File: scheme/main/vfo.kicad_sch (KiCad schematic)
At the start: 20 parts, among them Q1 BC847, U10 HCPL-817-50CE, U11 RS8551, U8 AMC1311, U9 RS8551

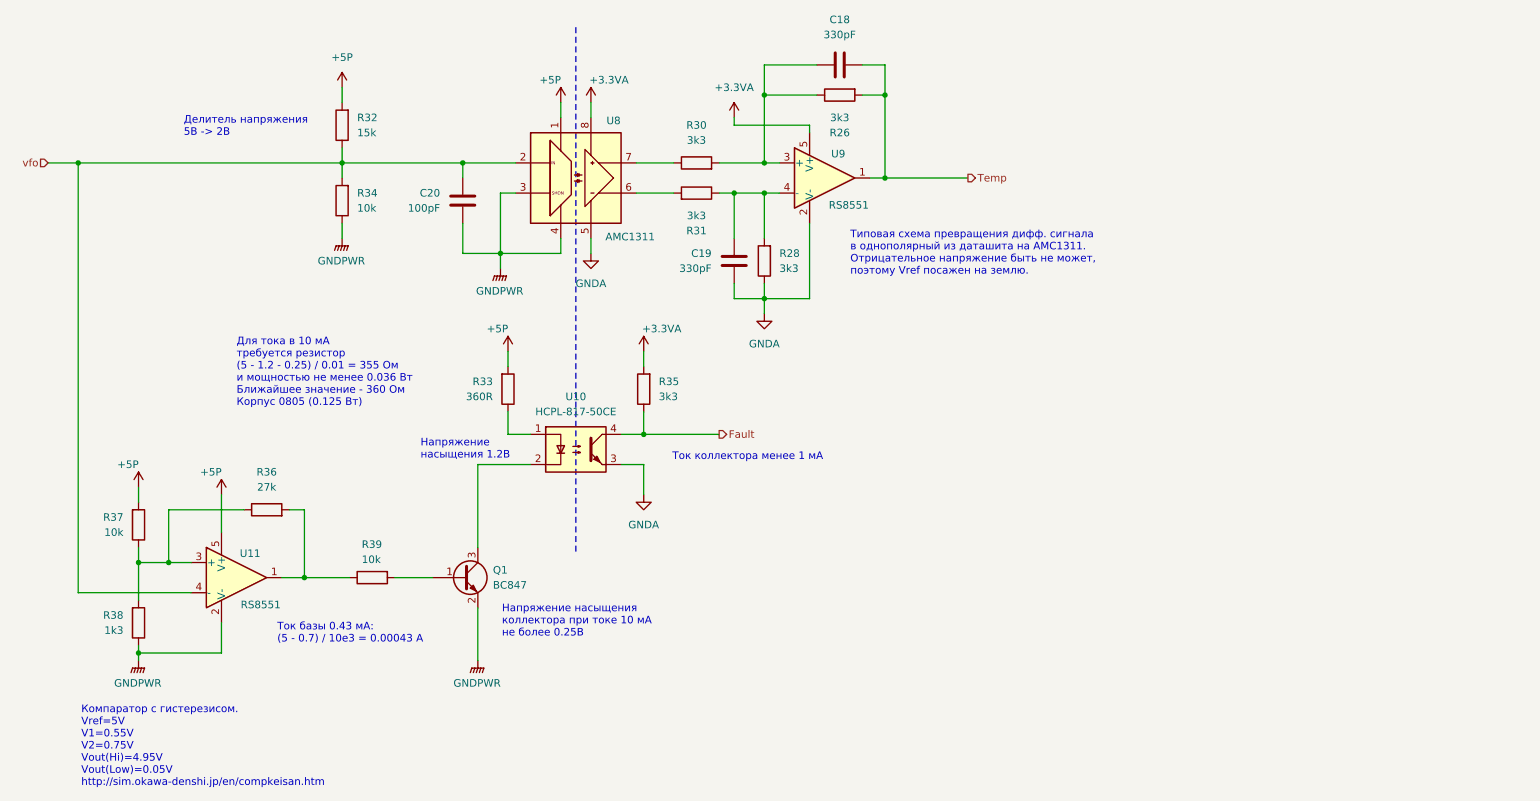
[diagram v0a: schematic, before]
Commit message: vdc meas scheme
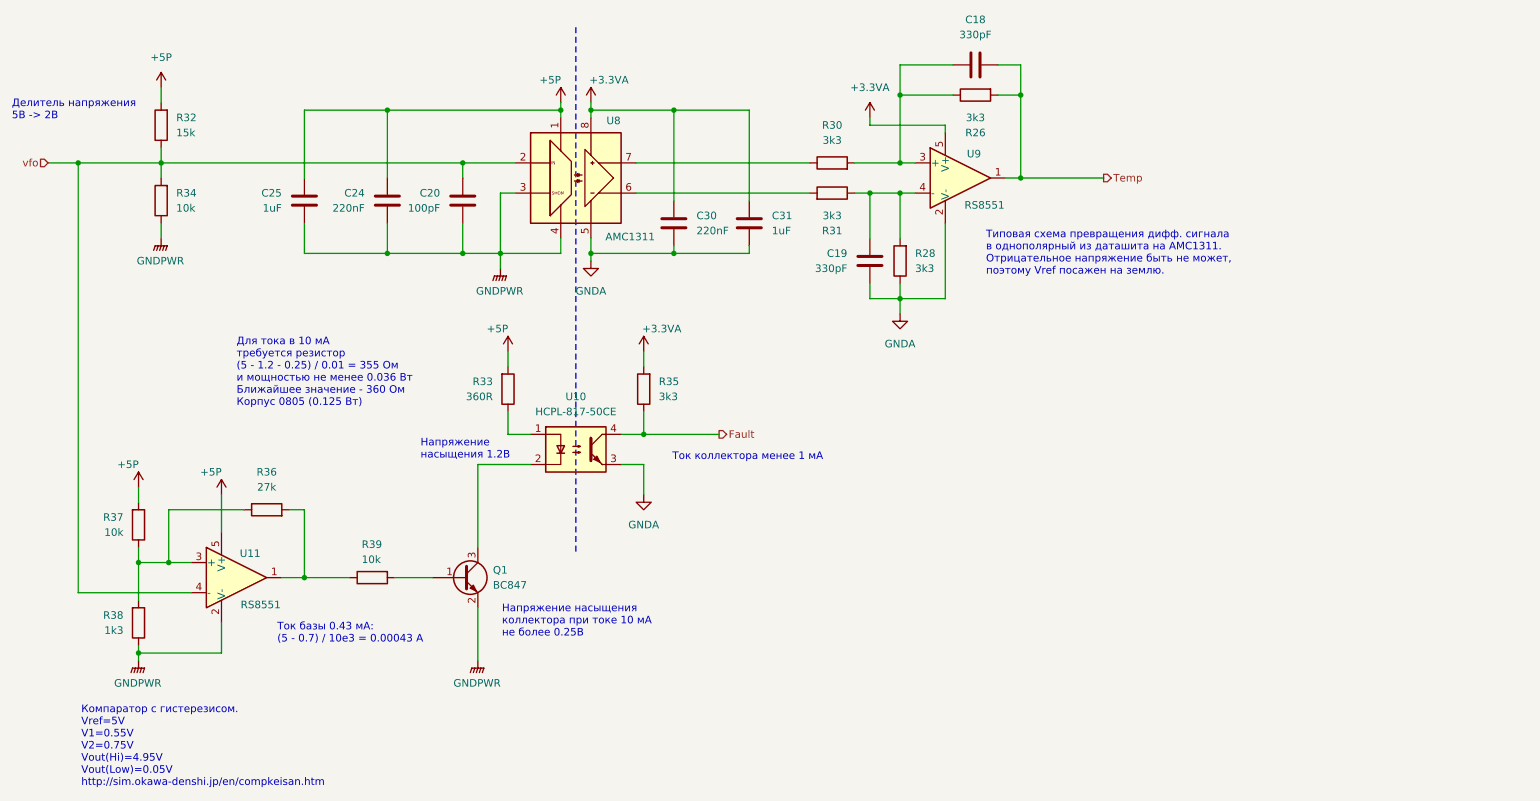
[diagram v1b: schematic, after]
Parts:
- added C24, C30: 220nF, Capacitor_SMD:C_0805_2012Metric, symbol Device:C
- added C25, C31: 1uF, Capacitor_SMD:C_0805_2012Metric, symbol Device:C
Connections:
- net +3.3VA: now also C30.1, C31.1
- net +5P: now also C24.1, C25.1
- net GNDA: now also C30.2, C31.2
- net GNDPWR: now also C24.2, C25.2
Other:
- moved on the sheet: C18, C19, R26, R28, R30, R31, R32, R34, U9

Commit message: added decoupling capacitors
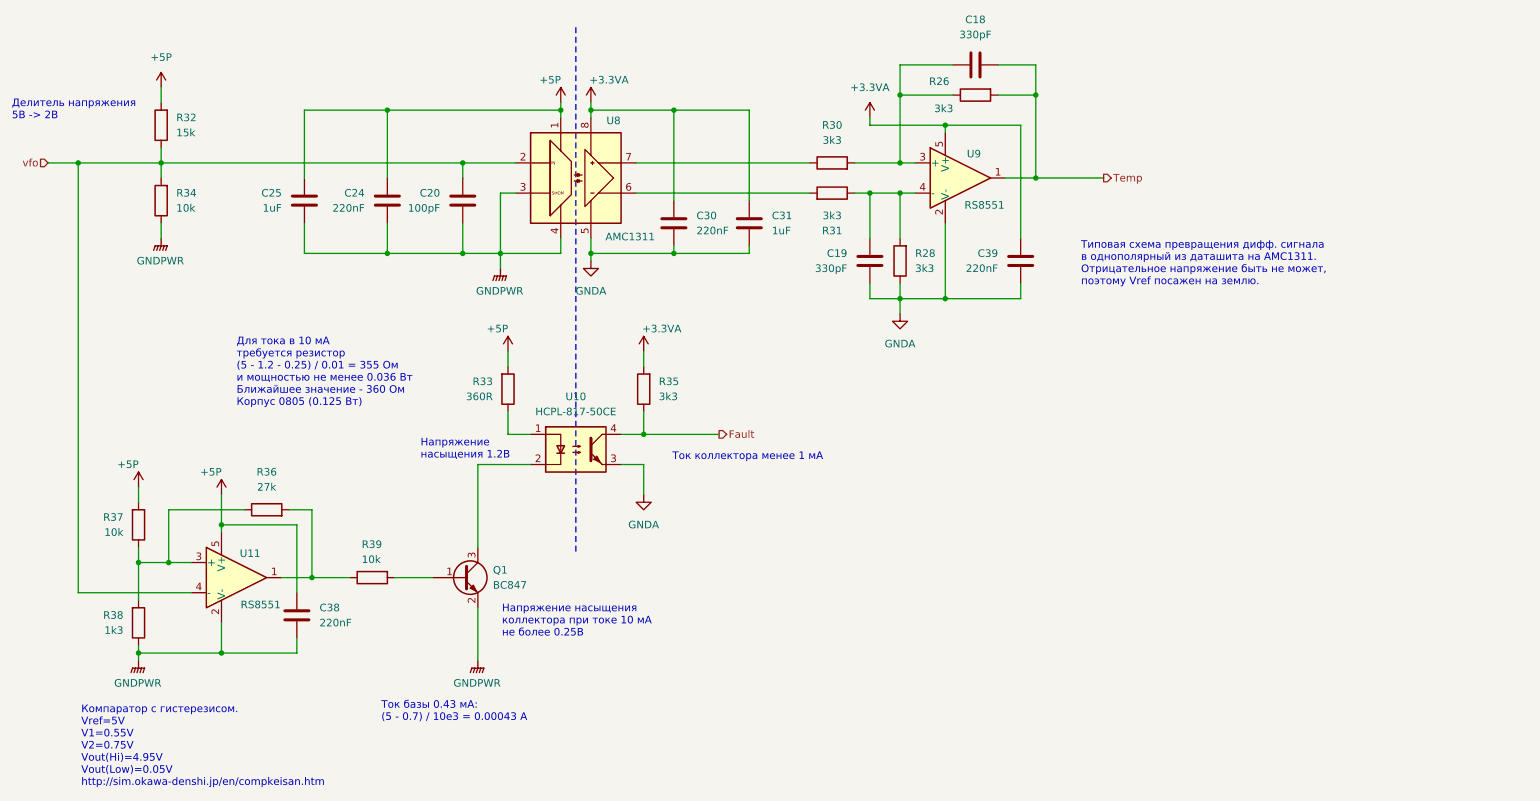
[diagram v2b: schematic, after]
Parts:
- added C38, C39: 220nF, Capacitor_SMD:C_0805_2012Metric, symbol Device:C
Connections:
- net +3.3VA: now also C39.1
- net +5P: now also C38.1
- net GNDA: now also C39.2
- net GNDPWR: now also C38.2

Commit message: power scheme in progress (added dc-dc)
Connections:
- net +3.3VA: no longer R35.2
- net GNDA: no longer U10.3
- new net +3.3V: R35.2
- new net GNDD: U10.3
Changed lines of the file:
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@@
+	)
+	(symbol
+		(lib_id "power:GNDD")
+		(at 138.43 101.6 0)
+		(unit 1)
+		(exclude_from_sim no)
+		(in_bom yes)
+		(on_board yes)
+		(dnp no)
+		(fields_autoplaced yes)
+		(property "Reference" "#PWR22"
+			(at 138.43 107.95 0)
+			(effects
+				(font
+					(size 1.27 1.27)
+				)
+				(hide yes)
+			)
+		)
+		(property "Value" "GNDD"
+			(at 138.43 105.41 0)
+			(effects
+				(font
+					(size 1.27 1.27)
+				)
+			)
+		)
+		(property "Footprint" ""
+			(at 138.43 101.6 0)
+			(effects
+				(font
+					(size 1.27 1.27)
+				)
+				(hide yes)
+			)
+		)
+		(property "Datasheet" ""
+			(at 138.43 101.6 0)
+			(effects
+				(font
+					(size 1.27 1.27)
+				)
+				(hide yes)
+			)
+		)
+		(property "Description" "Power symbol creates a global label with name \"GNDD\" , digital ground"
+			(at 138.43 101.6 0)
+			(effects
+				(font
+					(size 1.27 1.27)
+				)
+				(hide yes)
+			)
+		)
+		(pin "1"
+		)
+		(instances
+			(project ""
+				(path "/c11d1dbc-4db9-4712-8d1d-5f6f7086cded/5d407613-ca47-4478-86ea-137e1786be86/80738a43-c598-4f09-a725-55d3789b6a7d"
+					(reference "#PWR22")
+					(unit 1)
+				)
+			)
+		)
 	)
 	(symbol
@@
 	)
 	(symbol
-		(lib_id "power:GNDA")
-		(at 138.43 101.6 0)
+		(lib_id "power:+3.3V")
+		(at 138.43 77.47 0)
 		(unit 1)
 		(exclude_from_sim no)
@@
 		(fields_autoplaced yes)
 		(property "Reference" "#PWR24"
-			(at 138.43 107.95 0)
-			(effects
-				(font
-					(size 1.27 1.27)
-				)
-				(hide yes)
-			)
-		)
-		(property "Value" "GNDA"
-			(at 138.43 106.68 0)
+			(at 138.43 81.28 0)
+			(effects
+				(font
+					(size 1.27 1.27)
+				)
+				(hide yes)
+			)
+		)
+		(property "Value" "+3.3V"
+			(at 138.43 72.39 0)
 			(effects
 				(font
@@
 		)
 		(property "Footprint" ""
-			(at 138.43 101.6 0)
+			(at 138.43 77.47 0)
 			(effects
 				(font
@@
 		)
 		(property "Datasheet" ""
-			(at 138.43 101.6 0)
-			(effects
-				(font
-					(size 1.27 1.27)
-				)
-				(hide yes)
-			)
-		)
-		(property "Description" "Power symbol creates a global label with name \"GNDA\" , analog ground"
-			(at 138.43 101.6 0)
-			(effects
-				(font
-					(size 1.27 1.27)
-				)
-				(hide yes)
-			)
-		)
-		(pin "1"
-		)
-		(instances
-			(project "main"
+			(at 138.43 77.47 0)
+			(effects
+				(font
+					(size 1.27 1.27)
+				)
+				(hide yes)
+			)
+		)
+		(property "Description" "Power symbol creates a global label with name \"+3.3V\""
+			(at 138.43 77.47 0)
+			(effects
+				(font
+					(size 1.27 1.27)
+				)
+				(hide yes)
+			)
+		)
+		(pin "1"
+		)
+		(instances
+			(project ""
 				(path "/c11d1dbc-4db9-4712-8d1d-5f6f7086cded/5d407613-ca47-4478-86ea-137e1786be86/80738a43-c598-4f09-a725-55d3789b6a7d"
 					(reference "#PWR24")
@@
 					(unit 1)
 				)
-			)
-		)
-	)
-	(symbol
-		(lib_id "power:+3.3VA")
-		(at 138.43 77.47 0)
-		(unit 1)
-		(exclude_from_sim no)
-		(in_bom yes)
-		(on_board yes)
-		(dnp no)
-		(property "Reference" "#PWR22"
-			(at 138.43 81.28 0)
-			(effects
-				(font
-					(size 1.27 1.27)
-				)
-				(hide yes)
-			)
-		)
-		(property "Value" "+3.3VA"
-			(at 141.478 73.66 0)
-			(effects
-				(font
-					(size 1.27 1.27)
-				)
-			)
-		)
-		(property "Footprint" ""
-			(at 138.43 77.47 0)
-			(effects
-				(font
-					(size 1.27 1.27)
-				)
-				(hide yes)
-			)
-		)
-		(property "Datasheet" ""
-			(at 138.43 77.47 0)
-			(effects
-				(font
-					(size 1.27 1.27)
-				)
-				(hide yes)
-			)
-		)
-		(property "Description" "Power symbol creates a global label with name \"+3.3VA\""
-			(at 138.43 77.47 0)
-			(effects
-				(font
-					(size 1.27 1.27)
-				)
-				(hide yes)
-			)
-		)
-		(pin "1"
-		)
-		(instances
-			(project "main"
-				(path "/c11d1dbc-4db9-4712-8d1d-5f6f7086cded/5d407613-ca47-4478-86ea-137e1786be86/80738a43-c598-4f09-a725-55d3789b6a7d"
-					(reference "#PWR22")
-					(unit 1)
-				)

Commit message: separate hi power & signal gnd
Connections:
- net GNDD renamed GND
- net GNDPWR renamed GNDH

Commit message: boards schematic sheets & more
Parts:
- added R105, R106: 22R, Resistor_SMD:R_0805_2012Metric, symbol Device:R
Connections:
- net Fault: now also R106.2; no longer R35.1, U10.4
- net Temp: now also R105.2; no longer C18.1, R26.2, U9.1
- new net: C18.1, R105.1, R26.2, U9.1
- new net: R106.1, R35.1, U10.4
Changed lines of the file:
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@@
 	(paper "A4")
 	(junction
-		(at 204.47 48.26)
+		(at 138.43 91.44)
 		(diameter 0)
 		(color 0 0 0 0)
@@
 	)
 	(junction
+		(at 204.47 48.26)
+		(diameter 0)
+		(color 0 0 0 0)
+	)
+	(junction
 		(at 181.61 68.58)
 		(diameter 0)
@@
 	)
 	(junction
-		(at 138.43 91.44)
-		(diameter 0)
-		(color 0 0 0 0)
-	)
-	(junction
 		(at 107.95 45.72)
 		(diameter 0)
@@
 	(wire
 		(pts
-			(xy 138.43 91.44) (xy 151.13 91.44)
-		)
-		(stroke
-			(width 0)
-			(type default)
-		)
-	)
-	(wire
-		(pts
 			(xy 119.38 91.44) (xy 115.57 91.44)
 		)
@@
 	(wire
 		(pts
+			(xy 138.43 91.44) (xy 147.32 91.44)
+		)
+		(stroke
+			(width 0)
+			(type default)
+		)
+	)
+	(wire
+		(pts
 			(xy 143.51 36.83) (xy 129.54 36.83)
 		)
@@
 	(wire
 		(pts
+			(xy 214.63 48.26) (xy 217.17 48.26)
+		)
+		(stroke
+			(width 0)
+			(type default)
+		)
+	)
+	(wire
+		(pts
 			(xy 143.51 52.07) (xy 143.51 36.83)
 		)
@@
 	(wire
 		(pts
-			(xy 204.47 48.26) (xy 215.9 48.26)
+			(xy 184.15 45.72) (xy 181.61 45.72)
 		)
 		(stroke
@@
 	(wire
 		(pts
-			(xy 184.15 45.72) (xy 181.61 45.72)
+			(xy 189.23 68.58) (xy 181.61 68.58)
 		)
 		(stroke
@@
 	(wire
 		(pts
-			(xy 189.23 68.58) (xy 181.61 68.58)
+			(xy 95.25 55.88) (xy 95.25 60.96)
 		)
 		(stroke
@@
 	(wire
 		(pts
-			(xy 95.25 55.88) (xy 95.25 60.96)
+			(xy 43.18 45.72) (xy 57.15 45.72)
 		)
 		(stroke
@@
 	(wire
 		(pts
-			(xy 43.18 45.72) (xy 57.15 45.72)
+			(xy 154.94 91.44) (xy 157.48 91.44)
 		)
 		(stroke
@@
 	(wire
 		(pts
+			(xy 204.47 48.26) (xy 207.01 48.26)
+		)
+		(stroke
+			(width 0)
+			(type default)
+		)
+	)
+	(wire
+		(pts
 			(xy 80.01 125.73) (xy 80.01 128.27)
 		)
@@
 	(hierarchical_label "Temp"
 		(shape output)
-		(at 215.9 48.26 0)
+		(at 217.17 48.26 0)
 		(fields_autoplaced yes)
 		(effects
@@
 	(hierarchical_label "Fault"
 		(shape output)
-		(at 151.13 91.44 0)
+		(at 157.48 91.44 0)
 		(fields_autoplaced yes)
 		(effects
@@
 	)
 	(symbol
+		(lib_id "Device:R")
+		(at 151.13 91.44 90)
+		(unit 1)
+		(exclude_from_sim no)
+		(in_bom yes)
+		(on_board yes)
+		(dnp no)
+		(fields_autoplaced yes)
+		(property "Reference" "R106"
+			(at 151.13 85.09 90)
+			(effects
+				(font
+					(size 1.27 1.27)
+				)
+			)
+		)
+		(property "Value" "22R"
+			(at 151.13 87.63 90)
+			(effects
+				(font
+					(size 1.27 1.27)
+				)
+			)
+		)
+		(property "Footprint" "Resistor_SMD:R_0805_2012Metric"
+			(at 151.13 93.218 90)
+			(effects
+				(font
+					(size 1.27 1.27)
+				)
+				(hide yes)
+			)
+		)
+		(property "Datasheet" "~"
+			(at 151.13 91.44 0)
+			(effects
+				(font
+					(size 1.27 1.27)
+				)
+				(hide yes)
+			)
+		)
+		(property "Description" "Resistor"
+			(at 151.13 91.44 0)
+			(effects
+				(font
+					(size 1.27 1.27)
+				)
+				(hide yes)
+			)
+		)
+		(pin "1"
+		)
+		(pin "2"
+		)
+		(instances
+			(project "main"
+				(path "/c11d1dbc-4db9-4712-8d1d-5f6f7086cded/5d407613-ca47-4478-86ea-137e1786be86/80738a43-c598-4f09-a725-55d3789b6a7d"
+					(reference "R106")
+					(unit 1)
+				)
+			)
+		)
+	)
+	(symbol
 		(lib_id "main:GNDH")
 		(at 53.34 129.54 0)
@@
 					(unit 1)
 				)
+			)
+		)
+	)
+	(symbol
+		(lib_id "Device:R")
+		(at 210.82 48.26 90)
+		(unit 1)
+		(exclude_from_sim no)
+		(in_bom yes)
+		(on_board yes)
+		(dnp no)
+		(fields_autoplaced yes)
+		(property "Reference" "R105"
+			(at 210.82 41.91 90)
+			(effects
+				(font
+					(size 1.27 1.27)
+				)
+			)
+		)
+		(property "Value" "22R"
+			(at 210.82 44.45 90)
+			(effects
+				(font
+					(size 1.27 1.27)
+				)
+			)
+		)
+		(property "Footprint" "Resistor_SMD:R_0805_2012Metric"
+			(at 210.82 50.038 90)
+			(effects
+				(font
+					(size 1.27 1.27)
+				)
+				(hide yes)
+			)
+		)
+		(property "Datasheet" "~"
+			(at 210.82 48.26 0)
+			(effects
+				(font
+					(size 1.27 1.27)
+				)
+				(hide yes)
+			)
+		)
+		(property "Description" "Resistor"
+			(at 210.82 48.26 0)
+			(effects
+				(font
+					(size 1.27 1.27)
+				)
+				(hide yes)
+			)
+		)
+		(pin "1"
+		)
+		(pin "2"
+		)
+		(instances
+			(project "main"
+				(path "/c11d1dbc-4db9-4712-8d1d-5f6f7086cded/5d407613-ca47-4478-86ea-137e1786be86/80738a43-c598-4f09-a725-55d3789b6a7d"
+					(reference "R105")
+					(unit 1)
+				)
